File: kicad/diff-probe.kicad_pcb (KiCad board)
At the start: 2 copper layers, 50 x 12 mm, 29 parts, among them IC3 LMH6702, IC4 LMH6702, IC5 LMH6702, J3 HEADER-1X2CARD-EDGE, J4 CON-1X3-TAB-AMP-29173-3-NARROW, X2 SMA--BU-SMA-H

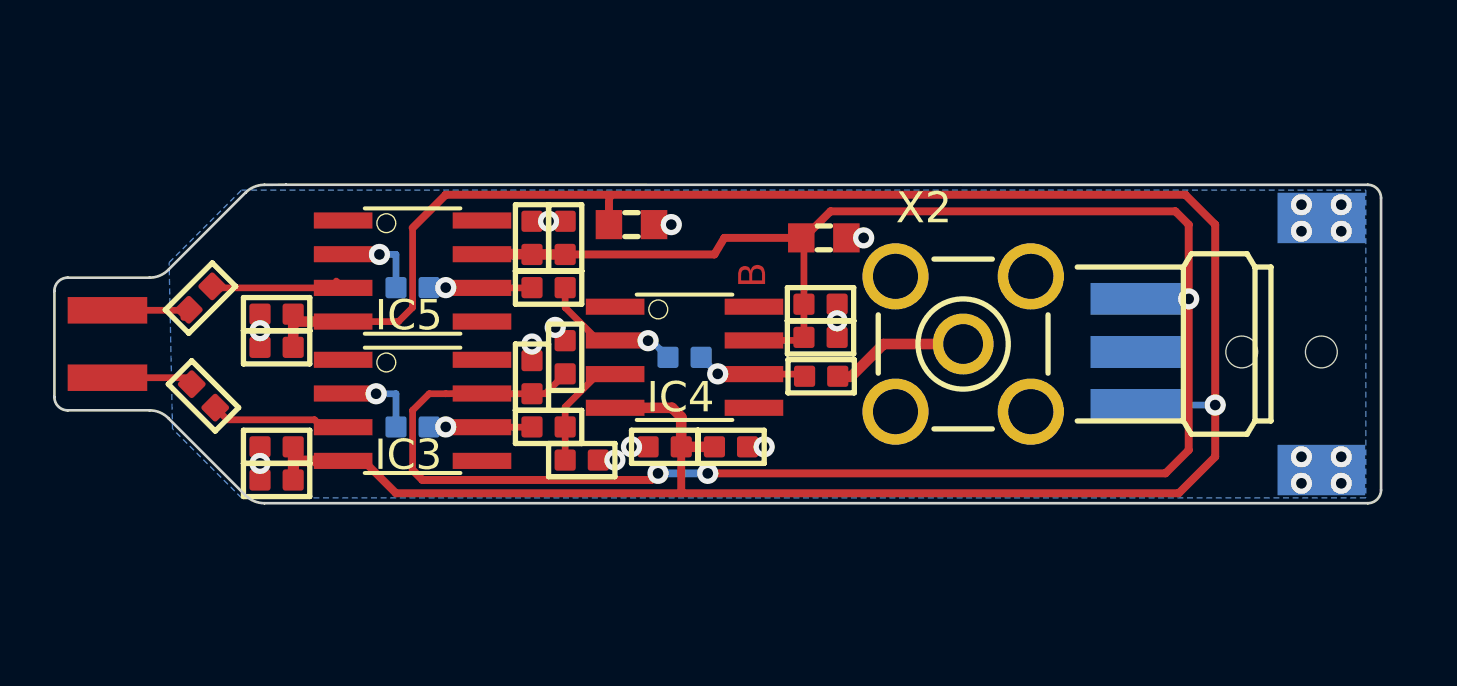
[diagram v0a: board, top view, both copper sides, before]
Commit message: Update original project - add the offset generated by the Auto Probe interface. Add the Auto-probe interface PCB.
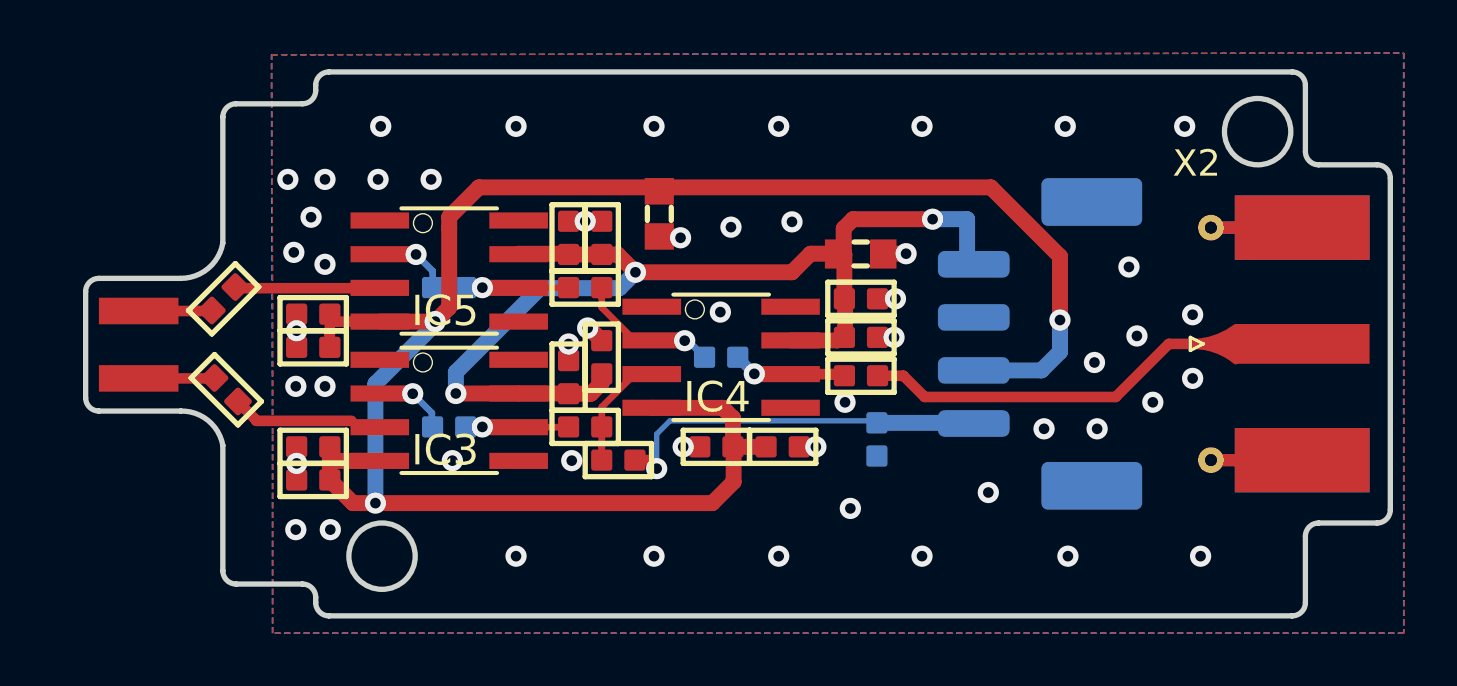
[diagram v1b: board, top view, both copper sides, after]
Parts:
- added C1: 100nF, Library:0402-SQUARE, B.Cu at (154.5, 101.6)
- C13, C14, C15, C16, C17, C18, C19, C20, C21, C22, C23, C24: value 10nF -> 100nF; footprint diff-probe:0402-SQUARE -> Library:0402-SQUARE
- C52, C54: footprint diff-probe:0603 -> Library:0603
- IC3, IC4, IC5: footprint diff-probe:SO08 -> Library:SO08
- J3: footprint diff-probe:CARD_EDGE_PADS-1X2 -> Library:CARD_EDGE_PADS-1X2
- J4: value CON-1X3-TAB-AMP-29173-3-NARROW -> Molex 502494-0470; footprint diff-probe:AMP-29173-3-NARROW -> Connector_Molex:Molex_CLIK-Mate_502494-0470_1x04-1MP_P2.00mm_Horizontal
- R20, R22, R26, R27, R28, R30, R32, R37, R38: footprint diff-probe:0402-SQUARE -> Library:0402-SQUARE
- X2: footprint diff-probe:BU-SMA-H -> Connector_Coaxial:SMA_Molex_73251-1153_EdgeMount_Horizontal_new
- moved J4 12.9 mm to (160.7, 98.0)
- moved X2 11.1 mm to (168.8, 98.0), turned to 180 degrees
- moved C23 1.95 mm to (148.4, 101.9)
- moved C24 1.95 mm to (150.9, 101.9)
- moved C17 1.54 mm to (153.9, 96.3)
- moved C18 1.52 mm to (153.9, 97.8)
- moved C52 1.52 mm to (153.9, 94.6)
- moved R30 1.50 mm to (153.9, 99.2)
- moved C13 1.38 mm to (142.9, 94.0)
- moved C14 1.38 mm to (144.1, 94.0)
- moved C15 1.38 mm to (144.1, 98.5)
- moved C16 1.38 mm to (142.9, 99.3)
- moved C19 1.38 mm to (133.3, 96.9)
- moved C20 1.38 mm to (133.3, 98.1)
- moved C21 1.38 mm to (133.3, 101.9)
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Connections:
- R26 pad P$2: GND -> /offset
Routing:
- net V+: track 82.2 -> 41.2 mm
- net /offset: track 0.00 -> 14.6 mm, vias 0 -> 1
- net V-: track 98.4 -> 84.5 mm, vias 1 -> 3
- net /OutPad: track 5.25 -> 17.2 mm
- net GND: track 15.5 -> 23.8 mm, vias 19 -> 51
- net /PosPad: track 4.44 -> 2.86 mm
- net /NegPad: track 4.11 -> 2.78 mm
- net /POSIN: track 5.94 -> 4.61 mm
- net /NEGMID: track 5.40 -> 6.58 mm
- net /POSMID: track 4.41 -> 5.16 mm
- net /NEGIN: track 6.08 -> 6.65 mm
- net /OUT: track 4.14 -> 4.66 mm
- added copper zone on F.Cu, net GND
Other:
- board size 50 x 12 mm -> 49.2 x 20.5 mm
- board text added: "0.2000 mm / 0.1778 mm"
- board text added: "0.3000 mm"
- board text added: "1.6000 mm"
- board text added: "13.50"
- board text added: "16.00"
- board text added: "18.10"
- board text added: "2"
- board text added: "2.25"
- board text added: "20.50"
- board text added: "3.20"
- board text added: "37.30"
- board text added: "38.00"
- board text added: "44.00"
- board text added: "49.1709 mm x 20.5000 mm"
- board text added: "BOARD CHARACTERISTICS"
- board text added: "Board Thickness:"
- board text added: "Board overall dimensions:"
- board text added: "Castellated pads:"
- board text added: "Copper Finish:"
- board text added: "Copper Layer Count:"
- board text added: "ENIG"
- board text added: "Edge card connectors:"
- board text added: "Impedance Control:"
- board text added: "Min hole diameter:"
- board text added: "Min track/spacing:"
- board text added: "No"
- board text added: "Plated Board Edge:"
- board text added: "Yes"
- board text added: "[.09]"
- board text added: "[.13]"
- board text added: "[.53]"
- board text added: "[.63]"
- board text added: "[.71]"
- board text added: "[.81]"
- board text added: "[1.47]"
- board text added: "[1.50]"
- board text added: "[1.73]"
- board text added: "∅2.50 [∅0.10]"
- board text removed: "B"
